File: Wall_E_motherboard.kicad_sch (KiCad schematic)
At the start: 57 parts, among them J1 Conn_01x02, SW3 SW_SPST, U2 STM32F411RCTx, U3 DRV8838, U6 BNO055, U7 DRV8838, Y1 25MHz, Y2 32.768kHz, Y3 32.768kHz

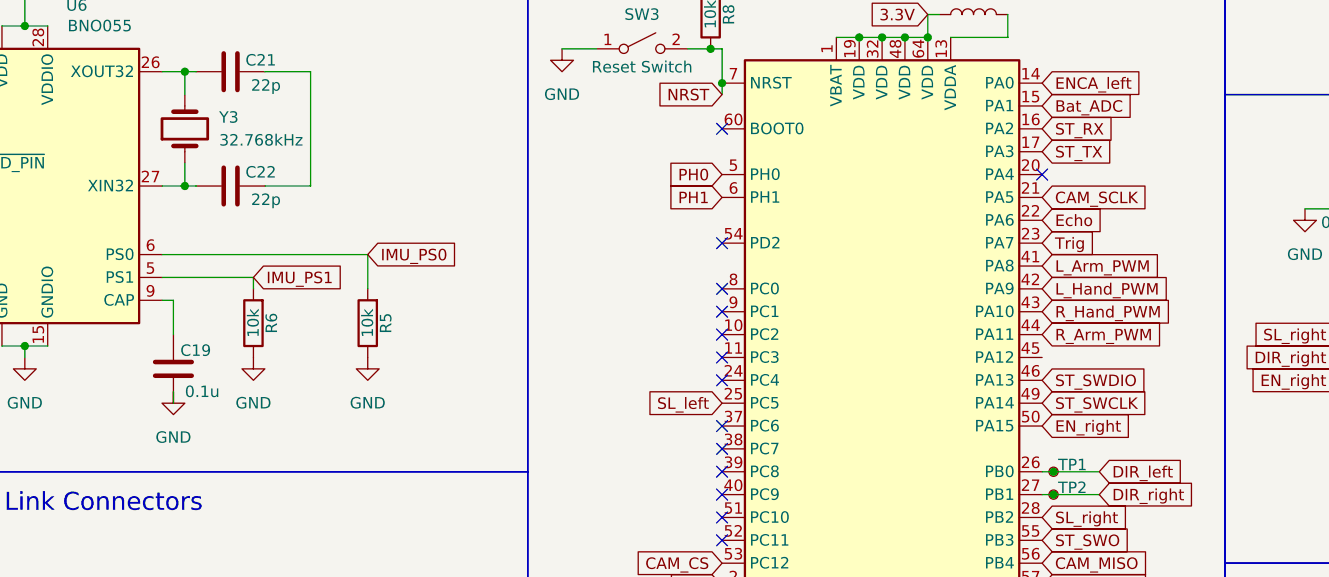
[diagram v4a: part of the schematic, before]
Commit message: Routing first draft complete
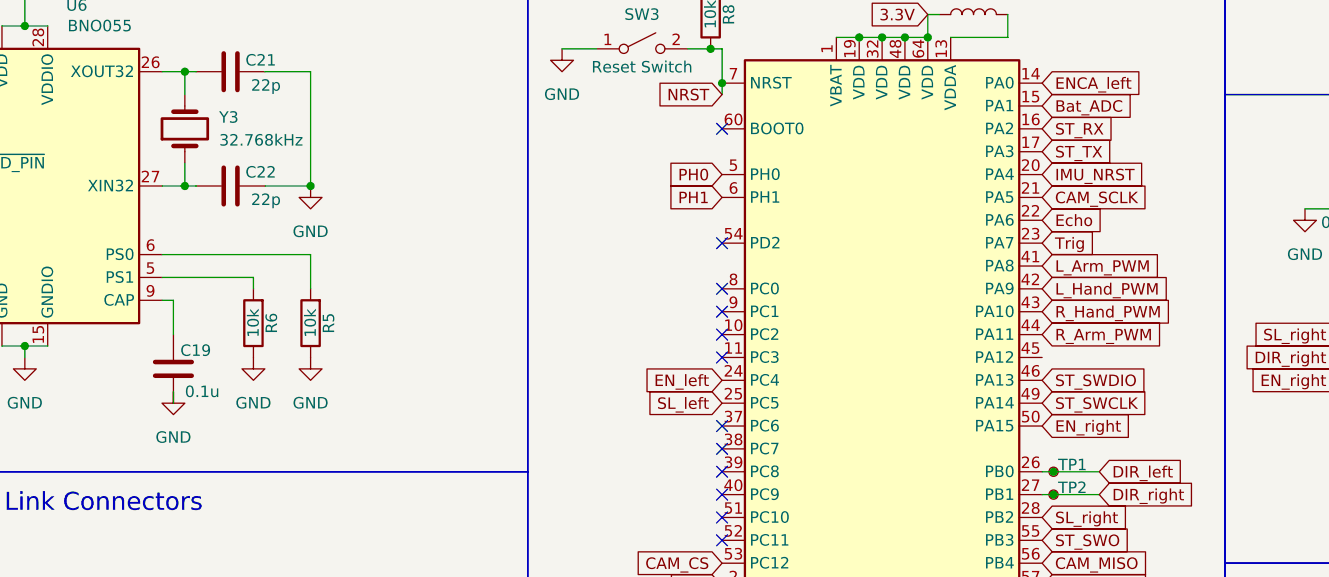
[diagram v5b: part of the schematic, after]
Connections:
- net EN_left: now also U2.24 (PC4)
- net GND: now also C21.2, C22.2
- net IMU_NRST: now also U2.20 (PA4)
- net IMU_PS0: no longer names the net of R5.2, U6.6 (PS0)
- net IMU_PS1: no longer names the net of R6.2, U6.5 (PS1)
- no-connect marks 18 -> 16
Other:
- moved on the sheet: R5
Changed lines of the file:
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@@
 	)
 	(junction
+		(at 87.63 78.74)
+		(diameter 0)
+		(color 0 0 0 0)
+	)
+	(junction
 		(at 209.55 81.28)
 		(diameter 0)
@@
 	)
 	(no_connect
-		(at 168.91 77.47)
-	)
-	(no_connect
 		(at 133.35 118.11)
 	)
@@
 	)
 	(no_connect
-		(at 133.35 100.33)
-	)
-	(no_connect
 		(at 133.35 95.25)
 	)
@@
 	(wire
 		(pts
-			(xy 93.98 90.17) (xy 93.98 86.36)
+			(xy 87.63 90.17) (xy 87.63 86.36)
 		)
 		(stroke
@@
 	(wire
 		(pts
-			(xy 93.98 86.36) (xy 71.12 86.36)
+			(xy 87.63 86.36) (xy 71.12 86.36)
 		)
 		(stroke
@@
 		)
 	)
+	(global_label "IMU_NRST"
+		(shape input)
+		(at 168.91 77.47 0)
+		(fields_autoplaced yes)
+		(effects
+			(font
+				(size 1.27 1.27)
+			)
+			(justify left)
+		)
+		(property "Intersheetrefs" "${INTERSHEET_REFS}"
+			(at 181.0271 77.47 0)
+			(effects
+				(font
+					(size 1.27 1.27)
+				)
+				(justify left)
+				(hide yes)
+			)
+		)
+	)
 	(global_label "Echo"
 		(shape input)
@@
 		)
 	)
-	(global_label "IMU_PS0"
-		(shape input)
-		(at 93.98 86.36 0)
-		(fields_autoplaced yes)
-		(effects
-			(font
-				(size 1.27 1.27)
-			)
-			(justify left)
-		)
-		(property "Intersheetrefs" "${INTERSHEET_REFS}"
-			(at 105.0085 86.36 0)
-			(effects
-				(font
-					(size 1.27 1.27)
-				)
-				(justify left)
-				(hide yes)
-			)
-		)
-	)
 	(global_label "ENCB_right"
 		(shape input)
@@
 		)
 	)
+	(global_label "EN_left"
+		(shape input)
+		(at 133.35 100.33 180)
+		(fields_autoplaced yes)
+		(effects
+			(font
+				(size 1.27 1.27)
+			)
+			(justify right)
+		)
+		(property "Intersheetrefs" "${INTERSHEET_REFS}"
+			(at 123.7125 100.33 0)
+			(effects
+				(font
+					(size 1.27 1.27)
+				)
+				(justify right)
+				(hide yes)
+			)
+		)
+	)
 	(global_label "PC14"
 		(shape input)
@@
 		)
 	)
-	(global_label "IMU_PS1"
-		(shape input)
-		(at 81.28 88.9 0)
-		(fields_autoplaced yes)
-		(effects
-			(font
-				(size 1.27 1.27)
-			)
-			(justify left)
-		)
-		(property "Intersheetrefs" "${INTERSHEET_REFS}"
-			(at 92.3085 88.9 0)
-			(effects
-				(font
-					(size 1.27 1.27)
-				)
-				(justify left)
-				(hide yes)
-			)
-		)
-	)
 	(global_label "SL_right"
 		(shape input)
@@
 	(symbol
 		(lib_id "power:GND")
+		(at 87.63 78.74 0)
+		(unit 1)
+		(exclude_from_sim no)
+		(in_bom yes)
+		(on_board yes)
+		(dnp no)
+		(fields_autoplaced yes)
+		(property "Reference" "#PWR07"
+			(at 87.63 85.09 0)
+			(effects
+				(font
+					(size 1.27 1.27)
+				)
+				(hide yes)
+			)
+		)
+		(property "Value" "GND"
+			(at 87.63 83.82 0)
+			(effects
+				(font
+					(size 1.27 1.27)
+				)
+			)
+		)
+		(property "Footprint" ""
+			(at 87.63 78.74 0)
+			(effects
+				(font
+					(size 1.27 1.27)
+				)
+				(hide yes)
+			)
+		)
+		(property "Datasheet" ""
+			(at 87.63 78.74 0)
+			(effects
+				(font
+					(size 1.27 1.27)
+				)
+				(hide yes)
+			)
+		)
+		(property "Description" "Power symbol creates a global label with name \"GND\" , ground"
+			(at 87.63 78.74 0)
+			(effects
+				(font
+					(size 1.27 1.27)
+				)
+				(hide yes)
+			)
+		)
+		(pin "1"
+		)
+		(instances
+			(project "Wall_E_motherboard"
+				(path "/9ae1092b-7010-45fe-ba45-fb6f2205b10c"
+					(reference "#PWR07")
+					(unit 1)
+				)
+			)
+		)
+	)
+	(symbol
+		(lib_id "power:GND")
 		(at 55.88 97.79 0)
 		(unit 1)
@@
 	(symbol
 		(lib_id "power:GND")
-		(at 93.98 97.79 0)
+		(at 87.63 97.79 0)
 		(unit 1)
 		(exclude_from_sim no)
@@
 		(fields_autoplaced yes)
 		(property "Reference" "#PWR049"
-			(at 93.98 104.14 0)
+			(at 87.63 104.14 0)
 			(effects
 				(font
@@
 		)
 		(property "Value" "GND"
-			(at 93.98 102.87 0)
+			(at 87.63 102.87 0)
 			(effects
 				(font
@@
 		)
 		(property "Footprint" ""
-			(at 93.98 97.79 0)
+			(at 87.63 97.79 0)
 			(effects
 				(font
@@
 		)
 		(property "Datasheet" ""
-			(at 93.98 97.79 0)
+			(at 87.63 97.79 0)
 			(effects
 				(font
@@
 		)
 		(property "Description" "Power symbol creates a global label with name \"GND\" , ground"
-			(at 93.98 97.79 0)
+			(at 87.63 97.79 0)
 			(effects
 				(font
@@
 	(symbol
 		(lib_id "Device:R")
-		(at 93.98 93.98 180)
+		(at 87.63 93.98 180)
 		(unit 1)
 		(exclude_from_sim no)
@@
 		(dnp no)
 		(property "Reference" "R5"
-			(at 96.012 93.98 90)
+			(at 89.662 93.98 90)
 			(effects
 				(font
@@
 		)
 		(property "Value" "10k"
-			(at 93.98 93.98 90)
+			(at 87.63 93.98 90)
 			(effects
 				(font
@@
 		)
 		(property "Footprint" "Resistor_SMD:R_0603_1608Metric"
-			(at 95.758 93.98 90)
+			(at 89.408 93.98 90)
 			(effects
 				(font
@@
 		)
 		(property "Datasheet" "~"
-			(at 93.98 93.98 0)
+			(at 87.63 93.98 0)
 			(effects
 				(font
@@
 		)
 		(property "Description" "Resistor"
-			(at 93.98 93.98 0)
+			(at 87.63 93.98 0)
 			(effects
 				(font
@@
 		)
 		(property "Sim.Device" ""
-			(at 93.98 93.98 0)
+			(at 87.63 93.98 0)
 			(effects
 				(font
@@
 		)
 		(property "Sim.Pins" ""
-			(at 93.98 93.98 0)
+			(at 87.63 93.98 0)
 			(effects
 				(font
@@
 		)
 		(property "Sim.Type" ""
-			(at 93.98 93.98 0)
+			(at 87.63 93.98 0)
 			(effects
 				(font

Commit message: Final commit before Charlie review
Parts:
- ArmL1, ArmR1, C11, C9, Camera1, HandL1, HandR1, J1, LeftMotor1, Range1, RightMotor1, STLink1, UART1: now not fitted
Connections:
- no-connect marks 16 -> 17
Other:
- note added: "Mounting Holes"
- moved on the sheet: H1, H2, H3, H4, R18, R19

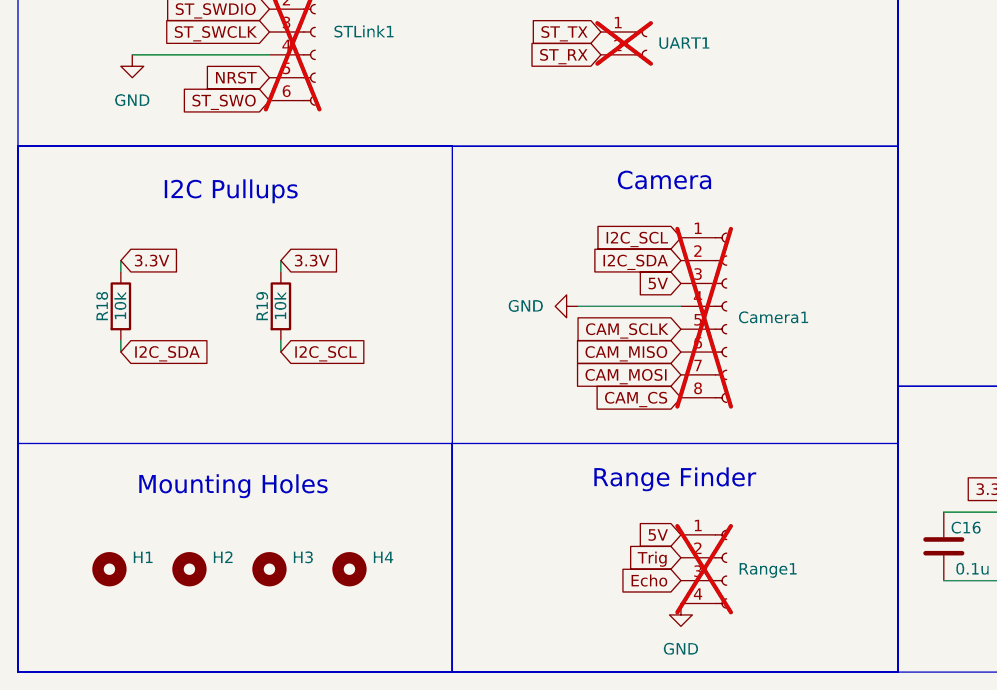
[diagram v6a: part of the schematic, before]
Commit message: added resistor divider to Echo pin
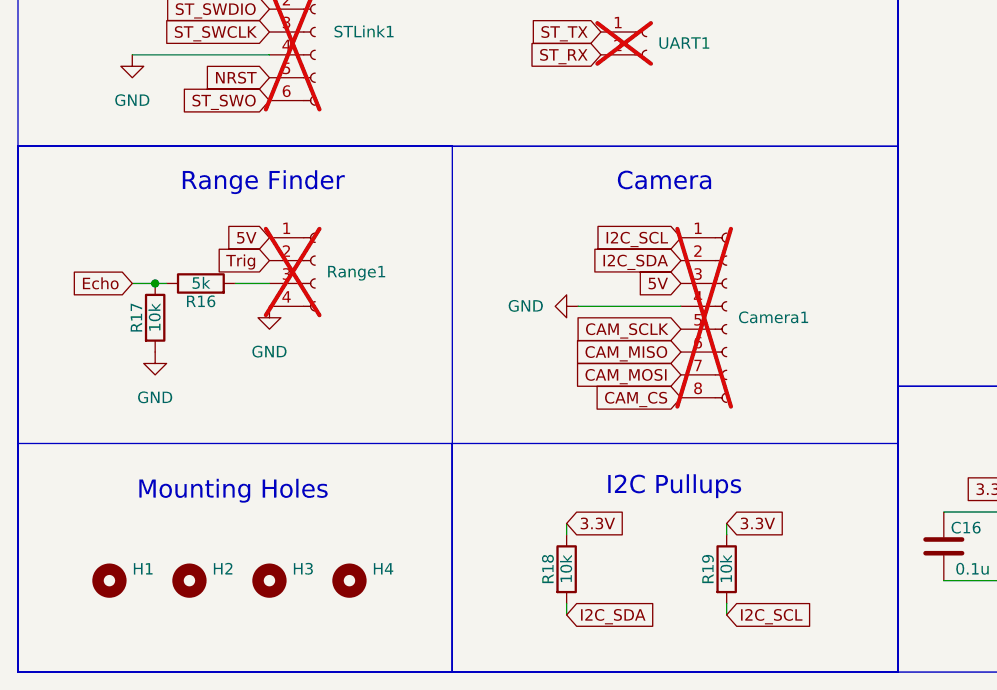
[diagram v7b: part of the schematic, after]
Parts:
- added R16: 5k, Resistor_SMD:R_0603_1608Metric, symbol Device:R
- added R17: 10k, Resistor_SMD:R_0603_1608Metric, symbol Device:R
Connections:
- net Echo: now also R16.1, R17.1; no longer Range1.3 (Pin_3)
- net GND: now also R17.2
- new net: R16.2, Range1.3 (Pin_3)
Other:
- moved on the sheet: H1, H2, H3, H4, R18, R19, Range1

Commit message: Final design before order
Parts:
- removed Y1: 25MHz, Crystal:Crystal_SMD_3225-4Pin_3.2x2.5mm, symbol Device:Crystal
- added C12, C13: 0.1u, Capacitor_SMD:C_0603_1608Metric, symbol Device:C
- added R20: 10k, Resistor_SMD:R_0603_1608Metric, symbol Device:R
- added Y1: 25MHz, Crystal:Crystal_SMD_3225-4Pin_3.2x2.5mm, symbol Device:Crystal_GND24
- C3: value 2.2u -> 4.7u
- R18, R19: value 10k -> 2.2k
- R3: value 500 -> 60
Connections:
- net GND: now also C12.2, C13.2, R20.1, Y1.2, Y1.4
- net NRST: now also C12.1
- net PH0: now also Y1.1
- net PH1: now also Y1.3
- net at L1.2, U2.13 (VDDA): now also C13.1
- net at U2.60 (BOOT0): now also R20.2
- no-connect marks 17 -> 16
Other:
- note added: "2.1V, 20mA"
- note removed: "20mA"
- moved on the sheet: C4, C5, C6, C7, R8, SW3, Y2
